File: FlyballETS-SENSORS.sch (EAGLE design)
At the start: 42 parts

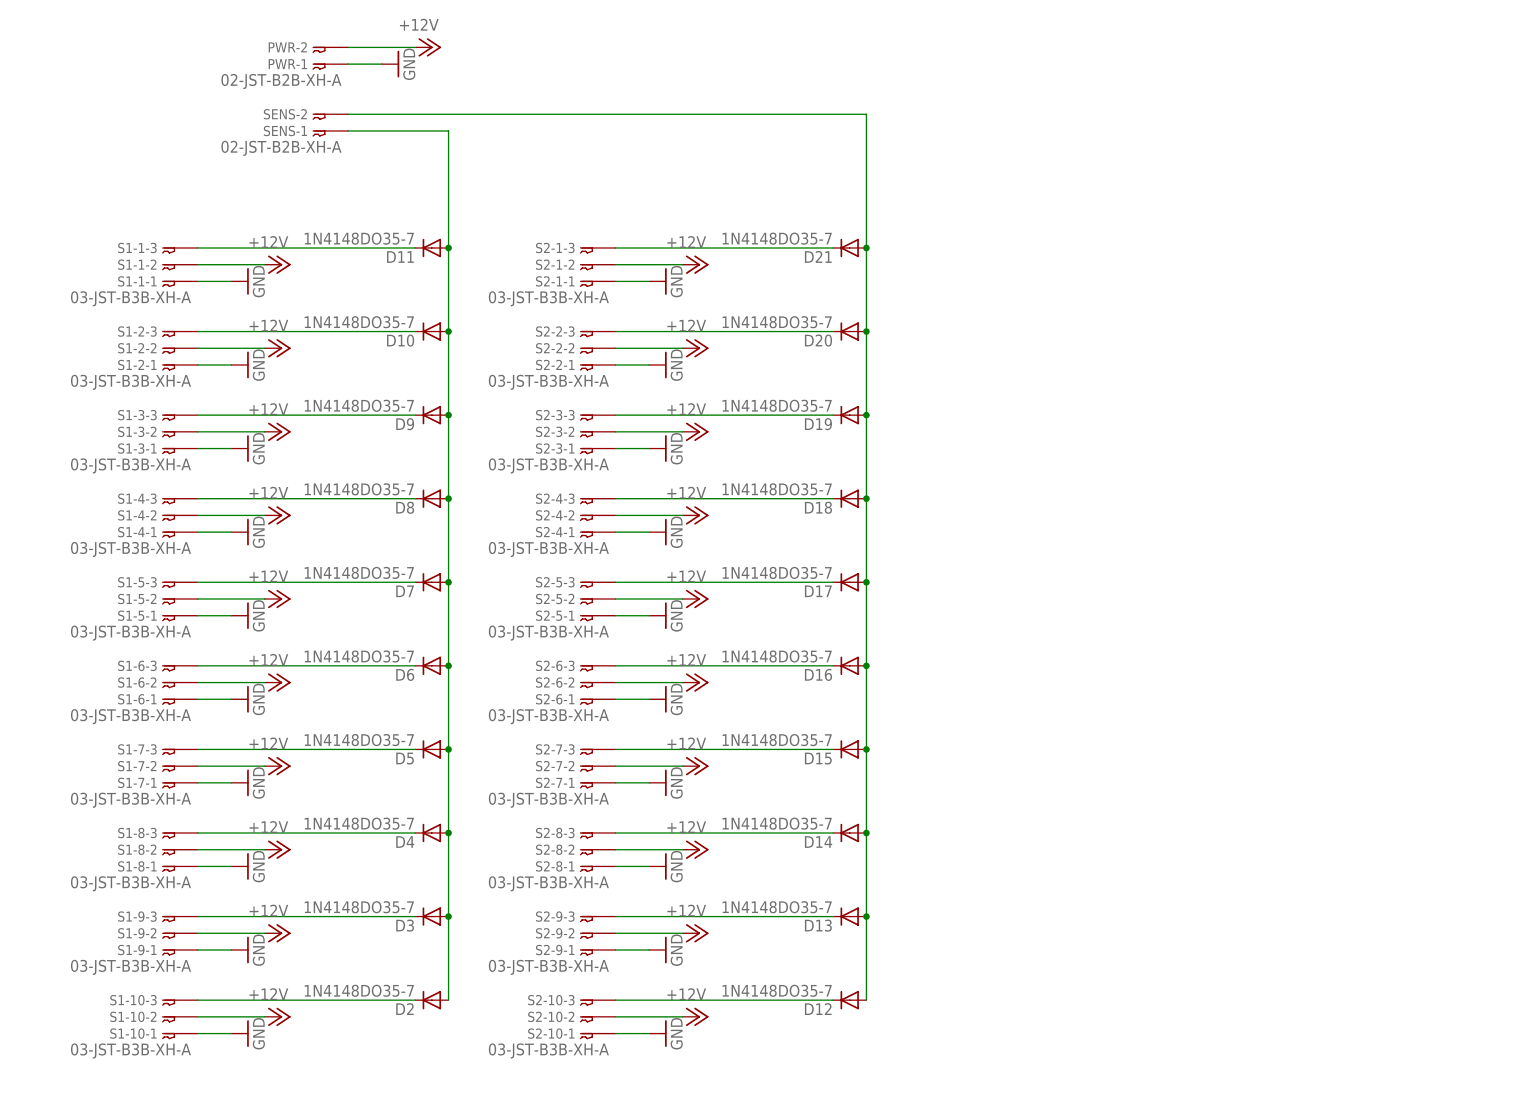
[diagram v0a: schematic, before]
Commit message: Updated drawings and added PNG exports
- Added frames around drawings to make it look neater
- Added PNG export files so people who don't have EAGLE can see
everything
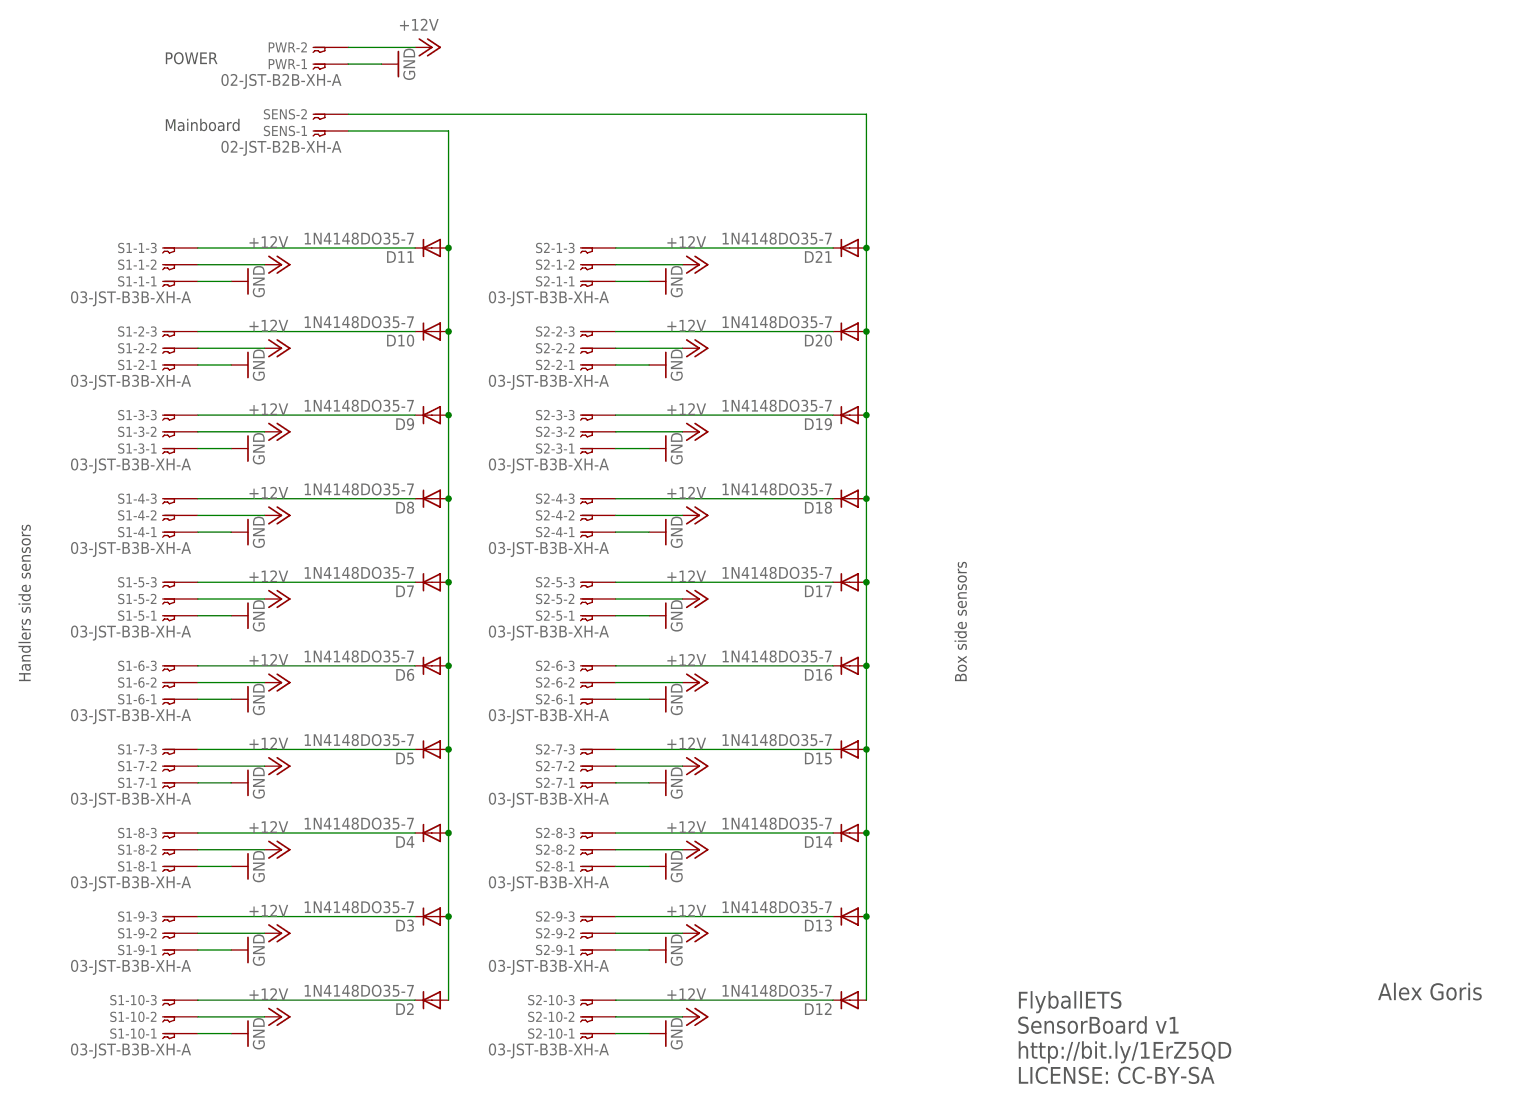
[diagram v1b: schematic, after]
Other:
- note added: "Alex Goris"
- note added: "Box side sensors"
- note added: "FlyballETS SensorBoard v1 http://bit.ly/1ErZ5QD LICENSE: CC-BY-SA"
- note added: "Handlers side sensors"
- note added: "Mainboard"
- note added: "POWER"
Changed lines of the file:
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@@
 <part name="D20" library="diode" deviceset="1N4148" device="DO35-7"/>
 <part name="D21" library="diode" deviceset="1N4148" device="DO35-7"/>
+<part name="FRAME1" library="frames" deviceset="A4L-LOC" device=""/>
 </parts>
 <sheets>
 <sheet>
 <plain>
+<text x="10.16" y="152.4" size="1.778" layer="97">POWER</text>
+<text x="10.16" y="142.24" size="1.778" layer="97">Mainboard</text>
+<text x="-10.16" y="58.42" size="1.778" layer="97" rot="R90">Handlers side sensors</text>
+<text x="132.08" y="58.42" size="1.778" layer="97" rot="R90">Box side sensors</text>
+<text x="139.7" y="-2.54" size="2.54" layer="97">FlyballETS
+SensorBoard v1
+http://bit.ly/1ErZ5QD
+LICENSE: CC-BY-SA</text>
+<text x="194.564" y="10.16" size="2.54" layer="97">Alex Goris</text>
 </plain>
 <instances>
@@
 <instance part="D20" gate="G$1" x="114.3" y="111.76" rot="R180"/>
 <instance part="D21" gate="G$1" x="114.3" y="124.46" rot="R180"/>
+<instance part="FRAME1" gate="G$1" x="-22.86" y="-10.16"/>
 </instances>
 <busses>
@@
 </schematic>
 </drawing>
+<compatibility>
+<note version="6.3" minversion="6.2.2" severity="warning">
+Since Version 6.2.2 text objects can contain more than one line,
+which will not be processed correctly with this version.
+</note>
+</compatibility>
 </eagle>

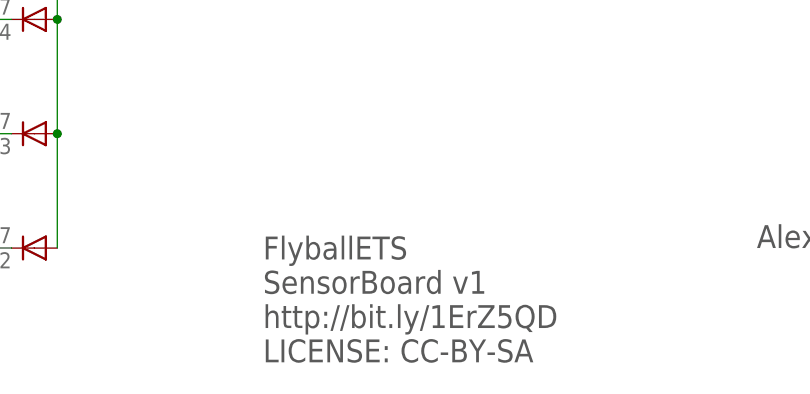
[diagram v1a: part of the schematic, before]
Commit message: v2 release of remaining boards.
- Lightsboard: Corrected swapped pin connections on L2 side and made
smaller
- Powerboard: Made smaller and added descriptions for LM2596 board
- Sensorboard: Made smaller
- All boards: Removed JST connector type names
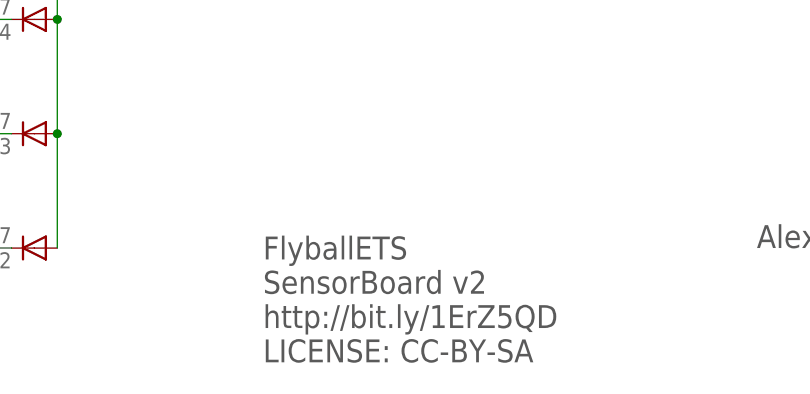
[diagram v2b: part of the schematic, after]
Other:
- note added: "FlyballETS SensorBoard v2 http://bit.ly/1ErZ5QD LICENSE: CC-BY-SA"
- note removed: "FlyballETS SensorBoard v1 http://bit.ly/1ErZ5QD LICENSE: CC-BY-SA"
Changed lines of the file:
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@@
 <?xml version="1.0" encoding="utf-8"?>
 <!DOCTYPE eagle SYSTEM "eagle.dtd">
-<eagle version="7.3.0">
+<eagle version="7.5.0">
 <drawing>
 <settings>
@@
 <setting verticaltext="up"/>
 </settings>
-<grid distance="2.54" unitdist="mm" unit="mm" style="lines" multiple="1" display="yes" altdistance="0.01" altunitdist="inch" altunit="inch"/>
+<grid distance="0.1" unitdist="inch" unit="inch" style="lines" multiple="1" display="no" altdistance="0.01" altunitdist="inch" altunit="inch"/>
 <layers>
 <layer number="1" name="Top" color="4" fill="1" visible="no" active="no"/>
@@
 <text x="132.08" y="58.42" size="1.778" layer="97" rot="R90">Box side sensors</text>
 <text x="139.7" y="-2.54" size="2.54" layer="97">FlyballETS
-SensorBoard v1
+SensorBoard v2
 http://bit.ly/1ErZ5QD
 LICENSE: CC-BY-SA</text>

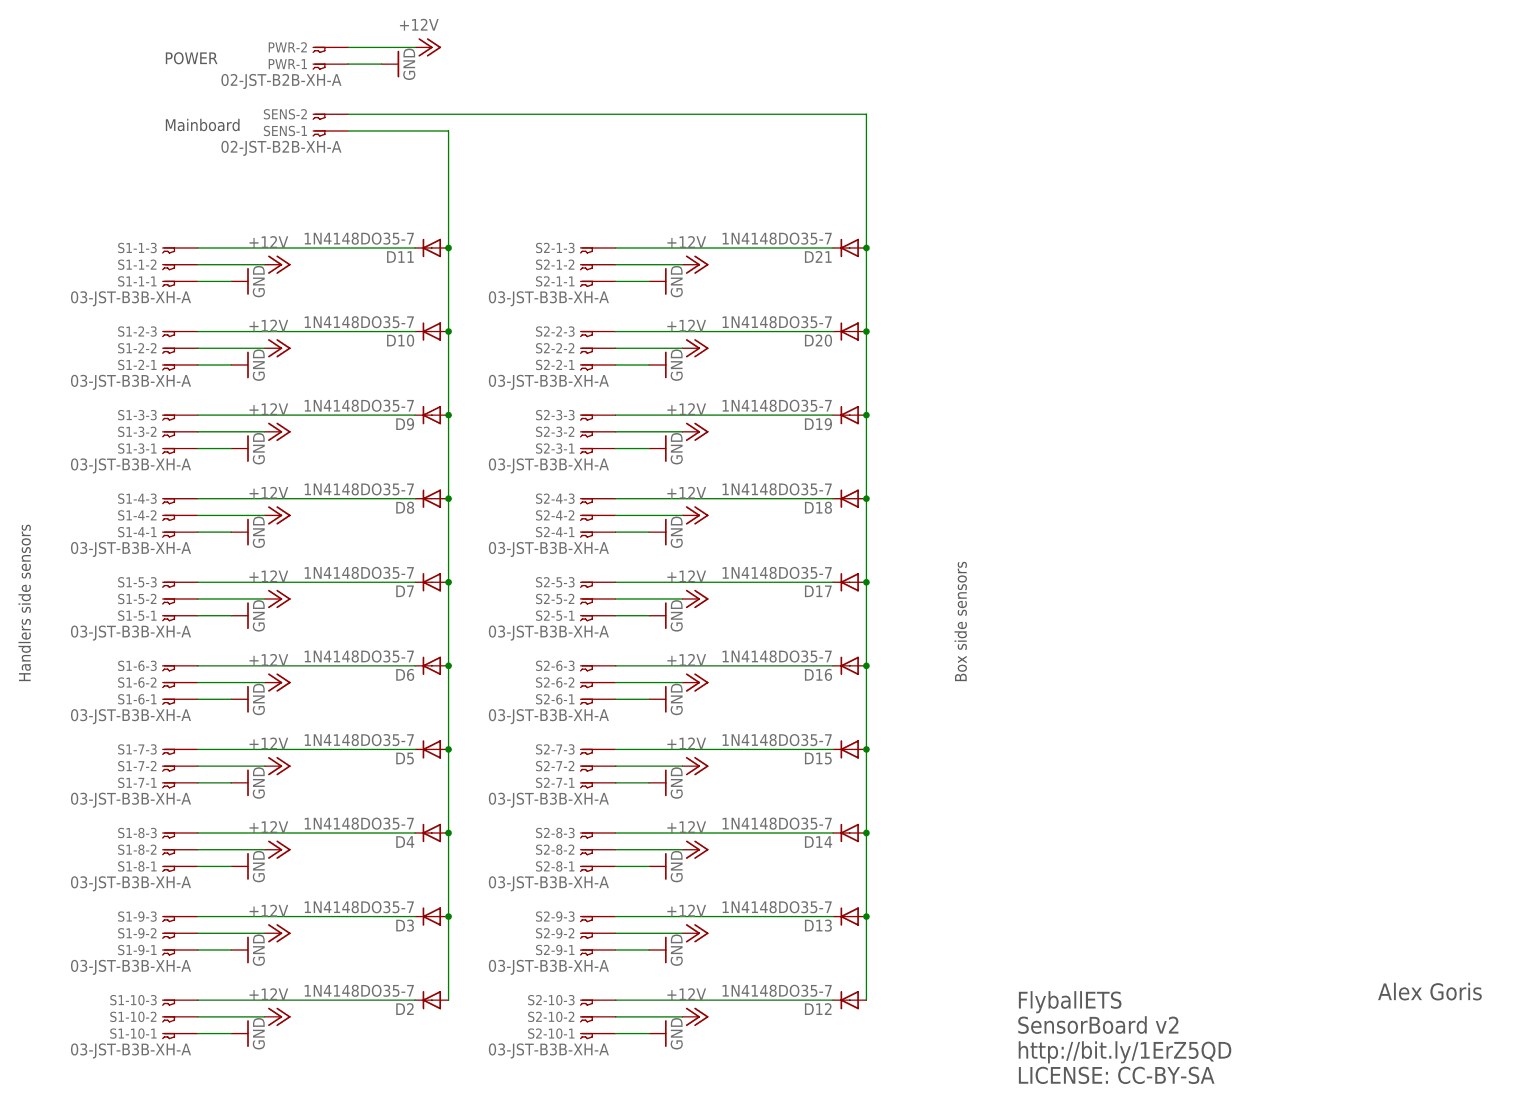
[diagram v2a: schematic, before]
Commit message: Fixed JST XH pin numbering
Updated bt_con-jst-xh.lbr library with swapped pin numbering.
Updated all board designs with updated library so they have the
connectors the right way around
Fixes #4
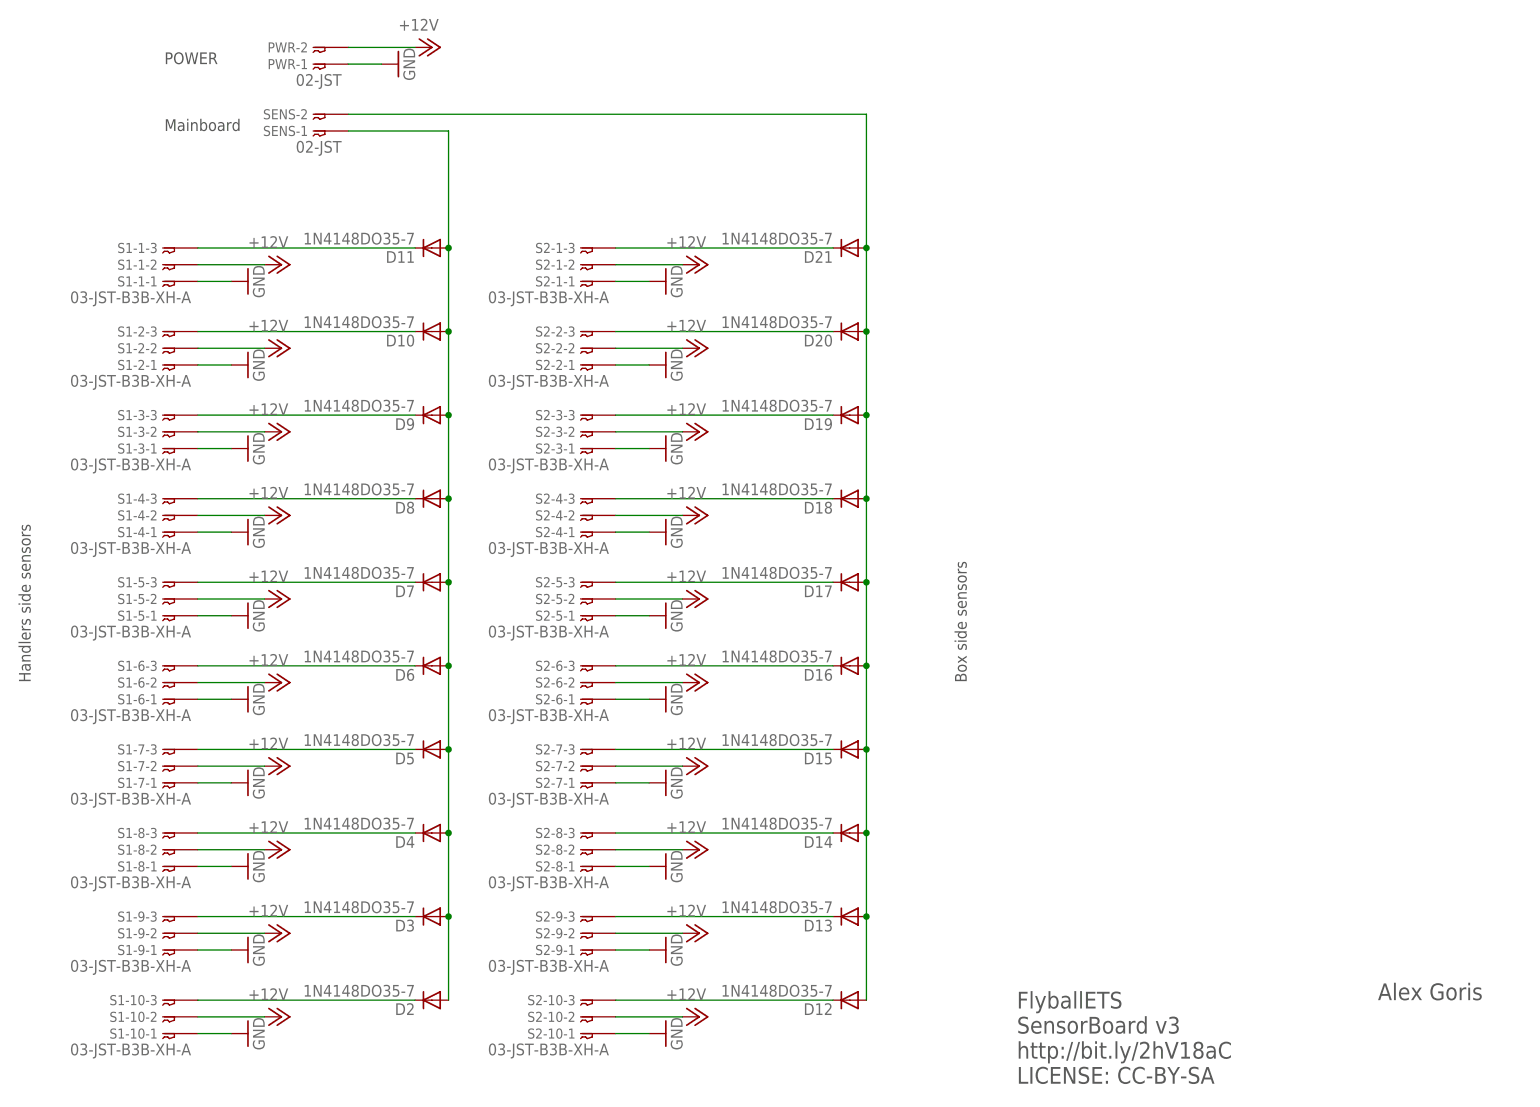
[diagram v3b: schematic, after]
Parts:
- PWR, SENS: value 02-JST-B2B-XH-A -> 02-JST; device bt_con-jst-xh:02-JST-B2B-XH-A -> bt_con-jst-xh:02-JST
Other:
- note added: "FlyballETS SensorBoard v3 http://bit.ly/2hV18aC LICENSE: CC-BY-SA"
- note removed: "FlyballETS SensorBoard v2 http://bit.ly/1ErZ5QD LICENSE: CC-BY-SA"
